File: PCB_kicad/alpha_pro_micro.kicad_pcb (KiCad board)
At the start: 2 copper layers, 192.9 x 59.5 mm, 72 parts, among them J1 Conn_01x03, J2 Conn_01x01_Female, J3 Conn_01x01_Female, J4 Conn_01x01_Female, J5 Conn_01x01_Female, J6 Conn_01x01_Female, J7 Conn_01x01_Female, J8 Conn_01x01_Female, J9 Conn_01x01_Female, K1 KEYSW, K10 KEYSW, K11 KEYSW, K12 KEYSW, K13 KEYSW, K14 KEYSW, K15 KEYSW, K16 KEYSW, K17 KEYSW, K18 KEYSW, K19 KEYSW, K2 KEYSW, K20 KEYSW, K21 KEYSW, K22 KEYSW, K23 KEYSW, K24 KEYSW, K25 KEYSW, K26 KEYSW, K27 KEYSW, K28 KEYSW, K3 KEYSW, K4 KEYSW, K5 KEYSW, K6 KEYSW, K7 KEYSW, K8 KEYSW, K9 KEYSW, SW1 SW_Push, U1 ProMicro

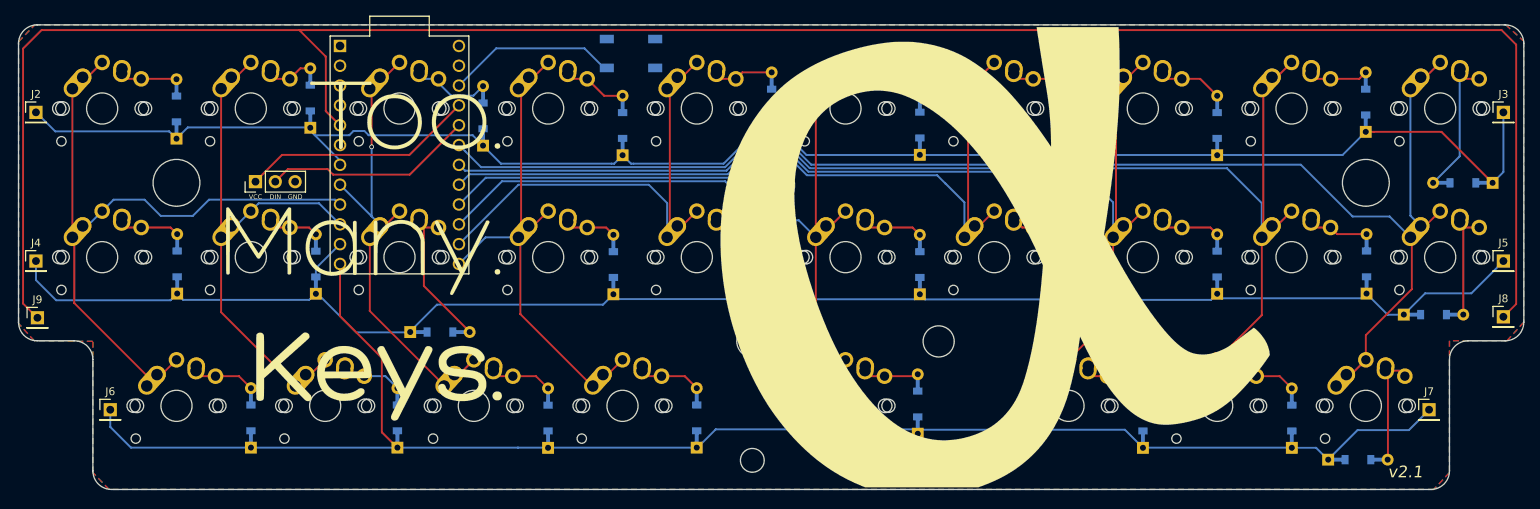
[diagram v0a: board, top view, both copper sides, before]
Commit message: Swapped switch footprint
Swapped switch footprint over to MX only, with LED support, and added support for LED driver and rest button.
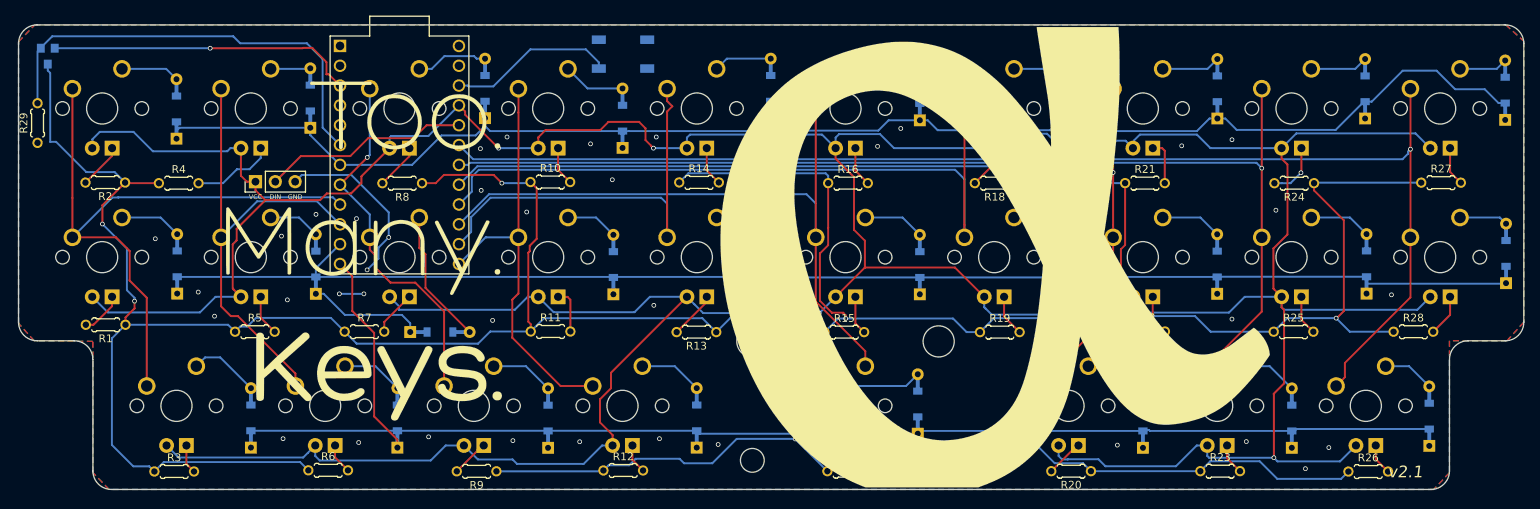
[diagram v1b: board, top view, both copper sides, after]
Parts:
- removed HC1, REF** (x2): MountingHole_6mm, Mounting_Holes:MountingHole_6mm
- removed J2, J3, J4, J5, J6, J7, J8, J9: Conn_01x01_Female, Connector_PinHeader_2.54mm:PinHeader_1x01_P2.54mm_Vertical
- added Q1: SMD-MOSFET-N-CH-60V-300MA-LOGIC-LEVEL-FET-2N7002_SOT-23_, OPL_Discrete_Semiconductor:SOT-23, B.Cu at (69.2, 102.8)
- added R1: SMD-RES-4.7K-5%-1_8W_0805_, OPL_Resistor:PR-D1.8_L3.3MM, F.Cu at (76.7, 137.2)
- added R10: SMD-RES-4.7K-5%-1_8W_0805_, OPL_Resistor:PR-D1.8_L3.3MM, F.Cu at (133.6, 119.0)
- added R11: SMD-RES-4.7K-5%-1_8W_0805_, OPL_Resistor:PR-D1.8_L3.3MM, F.Cu at (133.7, 138.1)
- added R12: SMD-RES-4.7K-5%-1_8W_0805_, OPL_Resistor:PR-D1.8_L3.3MM, F.Cu at (143.0, 155.9)
- added R13: SMD-RES-4.7K-5%-1_8W_0805_, OPL_Resistor:PR-D1.8_L3.3MM, F.Cu at (152.3, 138.2)
- added R14: SMD-RES-4.7K-5%-1_8W_0805_, OPL_Resistor:PR-D1.8_L3.3MM, F.Cu at (152.7, 119.0)
- added R15: SMD-RES-4.7K-5%-1_8W_0805_, OPL_Resistor:PR-D1.8_L3.3MM, F.Cu at (171.3, 138.2)
- added R16: SMD-RES-4.7K-5%-1_8W_0805_, OPL_Resistor:PR-D1.8_L3.3MM, F.Cu at (171.8, 119.1)
- added R17: SMD-RES-4.7K-5%-1_8W_0805_, OPL_Resistor:PR-D1.8_L3.3MM, F.Cu at (171.7, 156.0)
- added R18: SMD-RES-4.7K-5%-1_8W_0805_, OPL_Resistor:PR-D1.8_L3.3MM, F.Cu at (190.6, 119.1)
- added R19: SMD-RES-4.7K-5%-1_8W_0805_, OPL_Resistor:PR-D1.8_L3.3MM, F.Cu at (191.2, 138.2)
- added R2: SMD-RES-4.7K-5%-1_8W_0805_, OPL_Resistor:PR-D1.8_L3.3MM, F.Cu at (76.6, 119.0)
- added R20: SMD-RES-4.7K-5%-1_8W_0805_, OPL_Resistor:PR-D1.8_L3.3MM, F.Cu at (200.4, 156.0)
- added R21: SMD-RES-4.7K-5%-1_8W_0805_, OPL_Resistor:PR-D1.8_L3.3MM, F.Cu at (209.8, 119.1)
- added R22: SMD-RES-4.7K-5%-1_8W_0805_, OPL_Resistor:PR-D1.8_L3.3MM, F.Cu at (209.8, 138.1)
- added R23: SMD-RES-4.7K-5%-1_8W_0805_, OPL_Resistor:PR-D1.8_L3.3MM, F.Cu at (219.5, 156.0)
- added R24: SMD-RES-4.7K-5%-1_8W_0805_, OPL_Resistor:PR-D1.8_L3.3MM, F.Cu at (228.9, 119.1)
- added R25: SMD-RES-4.7K-5%-1_8W_0805_, OPL_Resistor:PR-D1.8_L3.3MM, F.Cu at (228.9, 138.1)
- added R26: SMD-RES-4.7K-5%-1_8W_0805_, OPL_Resistor:PR-D1.8_L3.3MM, F.Cu at (238.4, 156.1)
- added R27: SMD-RES-4.7K-5%-1_8W_0805_, OPL_Resistor:PR-D1.8_L3.3MM, F.Cu at (247.8, 119.0)
- added R28: SMD-RES-4.7K-5%-1_8W_0805_, OPL_Resistor:PR-D1.8_L3.3MM, F.Cu at (244.2, 138.1)
- added R29: SMD-RES-100K-5%-1_8W_0805_, OPL_Resistor:PR-D1.8_L3.3MM, F.Cu at (67.9, 111.4)
- added R3: SMD-RES-4.7K-5%-1_8W_0805_, OPL_Resistor:PR-D1.8_L3.3MM, F.Cu at (85.4, 156.1)
- added R4: SMD-RES-4.7K-5%-1_8W_0805_, OPL_Resistor:PR-D1.8_L3.3MM, F.Cu at (86.0, 119.1)
- added R5: SMD-RES-4.7K-5%-1_8W_0805_, OPL_Resistor:PR-D1.8_L3.3MM, F.Cu at (95.8, 138.1)
- added R6: SMD-RES-4.7K-5%-1_8W_0805_, OPL_Resistor:PR-D1.8_L3.3MM, F.Cu at (105.2, 155.9)
- added R7: SMD-RES-4.7K-5%-1_8W_0805_, OPL_Resistor:PR-D1.8_L3.3MM, F.Cu at (109.8, 138.1)
- added R8: SMD-RES-4.7K-5%-1_8W_0805_, OPL_Resistor:PR-D1.8_L3.3MM, F.Cu at (114.7, 119.1)
- added R9: SMD-RES-4.7K-5%-1_8W_0805_, OPL_Resistor:PR-D1.8_L3.3MM, F.Cu at (124.2, 156.0)
- K1, K10, K11, K12, K13, K14, K15, K16, K17, K18, K19, K2, K20, K21, K22, K23, K24, K26, K27, K28, K3, K4, K5, K6, K7, K8, K9: footprint keebio-parts:MX-Alps-Choc-1U-NoLED -> MX_Alps_Hybrid:MXOnly-1U
- K25: footprint keebio-parts:MX-Alps-Choc-2U-StabFlip -> MX_Alps_Hybrid:MXOnly-2U-ReversedStabilizers
- moved D10 13.1 mm to (256.0, 107.2), turned to 90 degrees
- moved D20 12.2 mm to (256.1, 128.1), turned to 90 degrees
- moved D28 10.7 mm to (246.2, 149.0), turned to 90 degrees
- moved D8 4.71 mm to (219.1, 107.0)
- moved D7 4.44 mm to (200.0, 107.2)
- moved D6 4.43 mm to (181.0, 107.2)
- moved D3 3.53 mm to (125.3, 107.0)
- moved D5 1.76 mm to (161.9, 107.0)
- moved D9 1.71 mm to (238.0, 107.0)
- moved SW1 1.03 mm to (142.9, 102.6)
- moved D4 0.94 mm to (142.9, 110.8)
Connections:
- K1 pad 1: Net-(D1-Pad2) -> /col0
- K1 pad 2: /col0 -> Net-(D1-Pad2)
- K10 pad 1: Net-(D10-Pad2) -> /col9
- K10 pad 2: /col9 -> Net-(D10-Pad2)
- K11 pad 1: Net-(D11-Pad2) -> /col0
- K11 pad 2: /col0 -> Net-(D11-Pad2)
- K12 pad 1: Net-(D12-Pad2) -> /col1
- K12 pad 2: /col1 -> Net-(D12-Pad2)
- K13 pad 1: Net-(D13-Pad2) -> /col2
- K13 pad 2: /col2 -> Net-(D13-Pad2)
- K14 pad 1: Net-(D14-Pad2) -> /col3
- K14 pad 2: /col3 -> Net-(D14-Pad2)
- K15 pad 1: Net-(D15-Pad2) -> /col4
- K15 pad 2: /col4 -> Net-(D15-Pad2)
- K16 pad 1: Net-(D16-Pad2) -> /col5
- K16 pad 2: /col5 -> Net-(D16-Pad2)
- K17 pad 1: Net-(D17-Pad2) -> /col6
- K17 pad 2: /col6 -> Net-(D17-Pad2)
- K18 pad 1: Net-(D18-Pad2) -> /col7
- K18 pad 2: /col7 -> Net-(D18-Pad2)
- K19 pad 1: Net-(D19-Pad2) -> /col8
- K19 pad 2: /col8 -> Net-(D19-Pad2)
- K2 pad 1: Net-(D2-Pad2) -> /col1
- K2 pad 2: /col1 -> Net-(D2-Pad2)
- K20 pad 1: Net-(D20-Pad2) -> /col9
- K20 pad 2: /col9 -> Net-(D20-Pad2)
- K21 pad 1: Net-(D21-Pad2) -> /col0
- K21 pad 2: /col0 -> Net-(D21-Pad2)
- K22 pad 1: Net-(D22-Pad2) -> /col1
- K22 pad 2: /col1 -> Net-(D22-Pad2)
- K23 pad 1: Net-(D23-Pad2) -> /col2
- K23 pad 2: /col2 -> Net-(D23-Pad2)
- K24 pad 1: Net-(D24-Pad2) -> /col3
- K24 pad 2: /col3 -> Net-(D24-Pad2)
- K25 pad 1: /col5 -> Net-(D25-Pad2)
- K25 pad 2: Net-(D25-Pad2) -> /col5
- K26 pad 1: Net-(D26-Pad2) -> /col7
- K26 pad 2: /col7 -> Net-(D26-Pad2)
- K27 pad 1: Net-(D27-Pad2) -> /col8
- K27 pad 2: /col8 -> Net-(D27-Pad2)
- K28 pad 1: Net-(D28-Pad2) -> /col9
- K28 pad 2: /col9 -> Net-(D28-Pad2)
- K3 pad 1: Net-(D3-Pad2) -> /col2
- K3 pad 2: /col2 -> Net-(D3-Pad2)
- K4 pad 1: Net-(D4-Pad2) -> /col3
- K4 pad 2: /col3 -> Net-(D4-Pad2)
- K5 pad 1: Net-(D5-Pad2) -> /col4
- K5 pad 2: /col4 -> Net-(D5-Pad2)
- K6 pad 1: Net-(D6-Pad2) -> /col5
- K6 pad 2: /col5 -> Net-(D6-Pad2)
- K7 pad 1: Net-(D7-Pad2) -> /col6
- K7 pad 2: /col6 -> Net-(D7-Pad2)
- K8 pad 1: Net-(D8-Pad2) -> /col7
- K8 pad 2: /col7 -> Net-(D8-Pad2)
- K9 pad 1: Net-(D9-Pad2) -> /col8
- K9 pad 2: /col8 -> Net-(D9-Pad2)
- U1 pad 6: Net-(U1-Pad6) -> /LED
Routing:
- net VCC: track 30.1 -> 595.4 mm, vias 0 -> 4
- net /LED_Out: track 0.00 -> 540.1 mm, vias 0 -> 7
- net /col_tmo: track 278.2 -> 0.00 mm
- net GND: track 0.00 -> 65.6 mm, vias 0 -> 44
- net /LED: track 0.00 -> 56.6 mm
- net /col8: track 158.2 -> 145.3 mm, vias 0 -> 1
- net /col7: track 138.6 -> 127.2 mm, vias 0 -> 1
- net Net-(K2-Pad4): track 0.00 -> 10.6 mm
- net Net-(D10-Pad2): track 18.2 -> 8.40 mm
- net /col9: track 174.2 -> 165.4 mm, vias 0 -> 1
- net Net-(D25-Pad2): track 7.29 -> 15.9 mm
- net /col2: track 55.1 -> 47.1 mm
- net /row2: track 204.4 -> 196.4 mm
- net /col5: track 97.7 -> 90.3 mm
- net Net-(K9-Pad4): track 0.00 -> 7.13 mm, vias 0 -> 1
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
